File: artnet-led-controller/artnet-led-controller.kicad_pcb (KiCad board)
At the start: 2 copper layers, 100 x 70 mm, 75 parts, among them J1 USB4125-GF-A, J10 SWD_DEBUG, J2 HR911105A, J3 VBAT JST-PH-2, J5 LED_OUT_1, J6 LED_OUT_2, J7 LED_OUT_3, J8 LED_OUT_4, J9 OLED_SSD1306, SW1 SW_Push, SW2 SW_Push, SW3 SW_Push, U1 RP2040, U2 W25Q16JVSSIQ, U3 W5500, U4 SN74AHCT125, U5 TP4056, U6 MT3608, U7 AMS1117-3.3, Y1 12MHz, Y2 25MHz

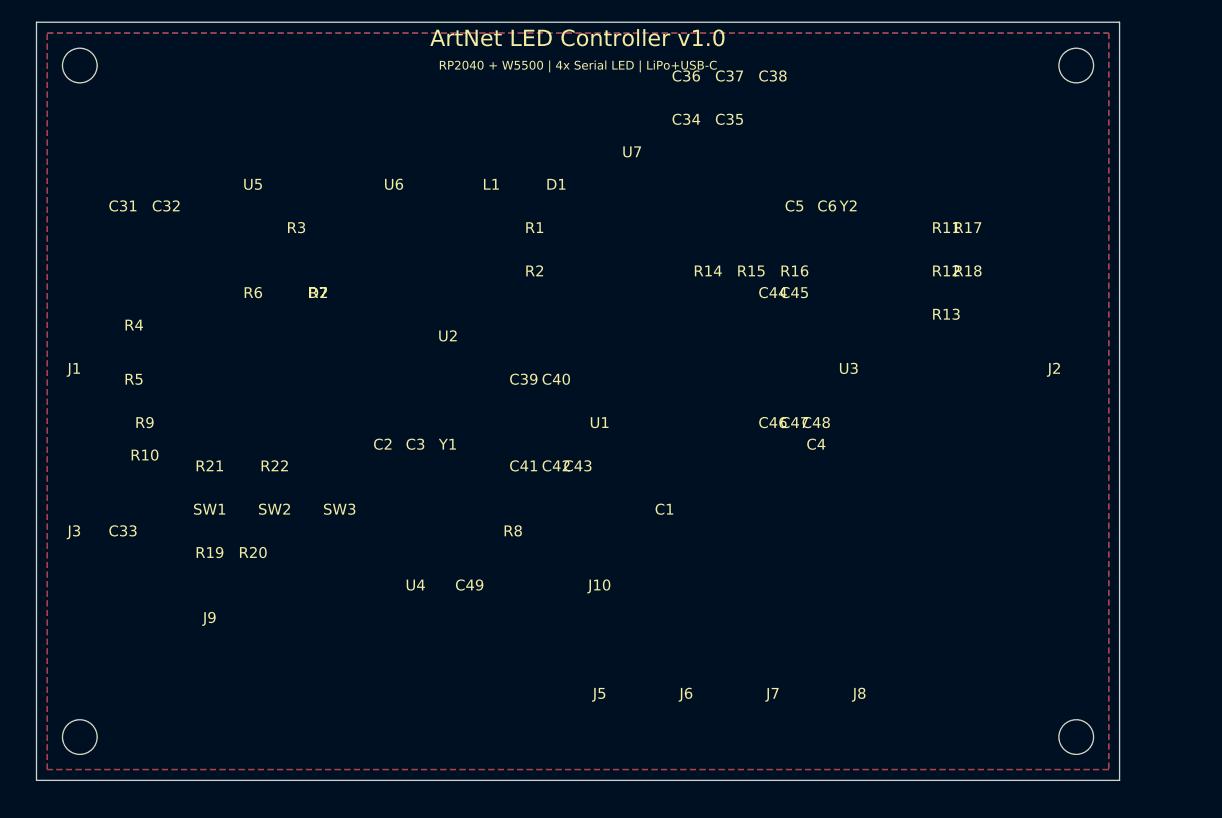
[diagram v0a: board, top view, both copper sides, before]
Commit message: Redesign controller around RP2354A
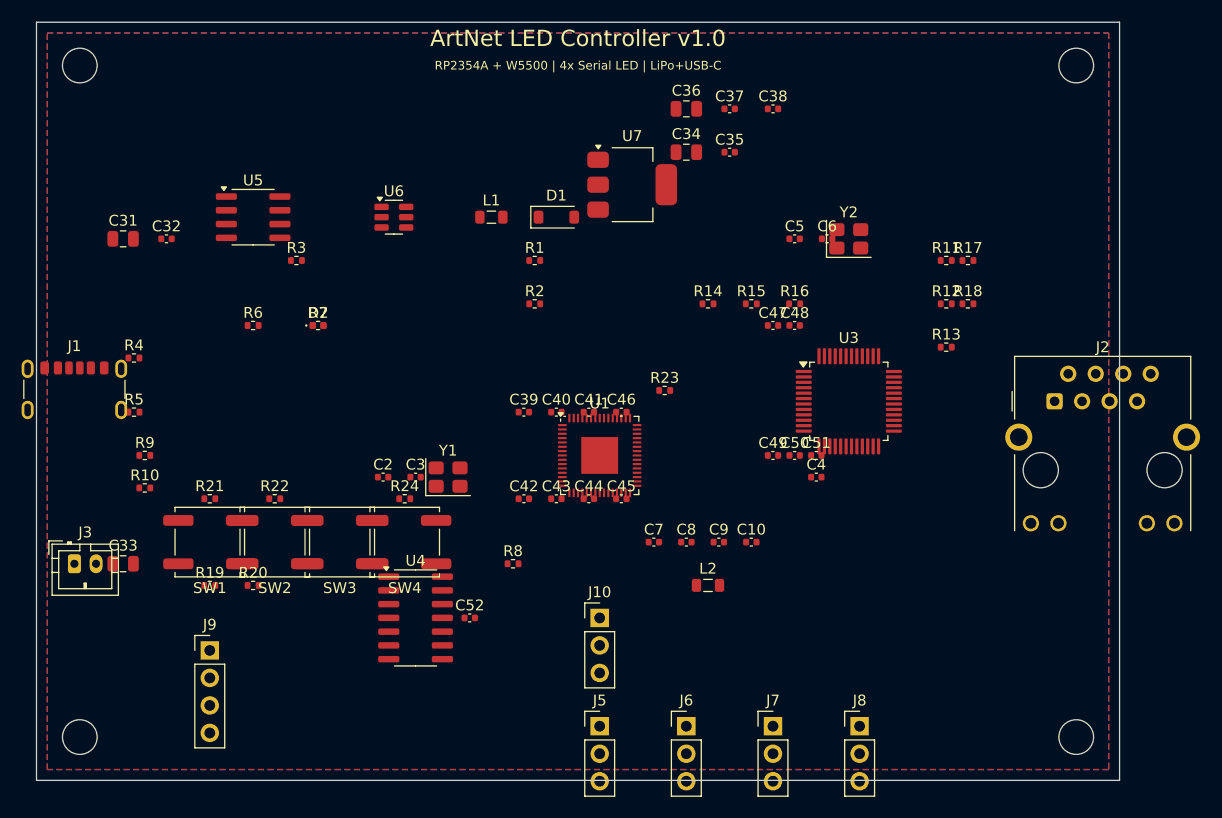
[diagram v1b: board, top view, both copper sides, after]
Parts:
- removed C1: 100nF, Capacitor_SMD:C_0402_1005Metric
- removed U2: W25Q16JVSSIQ, Package_SO:SOIC-8_3.9x4.9mm_P1.27mm
- added C10: 4.7uF, Capacitor_SMD:C_0402_1005Metric, F.Cu at (66.0, 48.0)
- added C50: 100nF, Capacitor_SMD:C_0402_1005Metric, F.Cu at (70.0, 40.0)
- added C51: 4.7uF, Capacitor_SMD:C_0402_1005Metric, F.Cu at (72.0, 40.0)
- added C52: 100nF, Capacitor_SMD:C_0402_1005Metric, F.Cu at (40.0, 55.0)
- added C7: 4.7uF, Capacitor_SMD:C_0402_1005Metric, F.Cu at (57.0, 48.0)
- added C8: 100nF, Capacitor_SMD:C_0402_1005Metric, F.Cu at (60.0, 48.0)
- added C9: 4.7uF, Capacitor_SMD:C_0402_1005Metric, F.Cu at (63.0, 48.0)
- added L2: 3.3uH, Inductor_SMD:L_0805_2012Metric, F.Cu at (62.0, 52.0)
- added R23: 33, Resistor_SMD:R_0402_1005Metric, F.Cu at (58.0, 34.0)
- added R24: 1k, Resistor_SMD:R_0402_1005Metric, F.Cu at (34.0, 44.0)
- added SW4: SW_Push, Button_Switch_SMD:SW_Push_1P1T_NO_CK_KSC7xxJ, F.Cu at (34.0, 48.0)
- C43: value 1uF -> 100nF
- C46: value 100nF -> 4.7uF
- C48: value 4.7uF -> 100nF
- J1: footprint Connector_USB:USB_C_Receptacle_GCT_USB4125_1x_1614 -> Connector_USB:USB_C_Receptacle_GCT_USB4125-xx-x_6P_TopMnt_Horizontal
- J2: footprint Connector_RJ:RJ45_Amphenol_54602-x08_Horizontal -> Connector_RJ:RJ45_Hanrun_HR911105A_Horizontal
- SW1, SW2, SW3: footprint Button_Switch_SMD:SW_Push_1P1T_NO_Vertical_Straight_PadInPin_CK_KSC741J -> Button_Switch_SMD:SW_Push_1P1T_NO_CK_KSC7xxJ
- U1: value RP2040 -> RP2354A; footprint Package_DFN_QFN:QFN-56-1EP_7x7mm_P0.4mm_EP3.2x3.2mm -> Package_DFN_QFN:QFN-60-1EP_7x7mm_P0.4mm_EP3.4x3.4mm
- moved C49 31.8 mm to (68.0, 40.0)
- moved C44 23.3 mm to (51.0, 44.0)
- moved C45 22.6 mm to (54.0, 44.0)
- moved C46 14.6 mm to (54.0, 36.0)
- moved C47 12.2 mm to (68.0, 28.0)
- moved C48 12.2 mm to (70.0, 28.0)
- moved C41 10.0 mm to (51.0, 36.0)
- moved C42 3.00 mm to (45.0, 44.0)
- moved C43 2.00 mm to (48.0, 44.0)
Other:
- board text added: "RP2354A + W5500 | 4x Serial LED | LiPo+USB-C"
- board text removed: "RP2040 + W5500 | 4x Serial LED | LiPo+USB-C"

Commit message: Clean PCB DRC and rotate RJ45
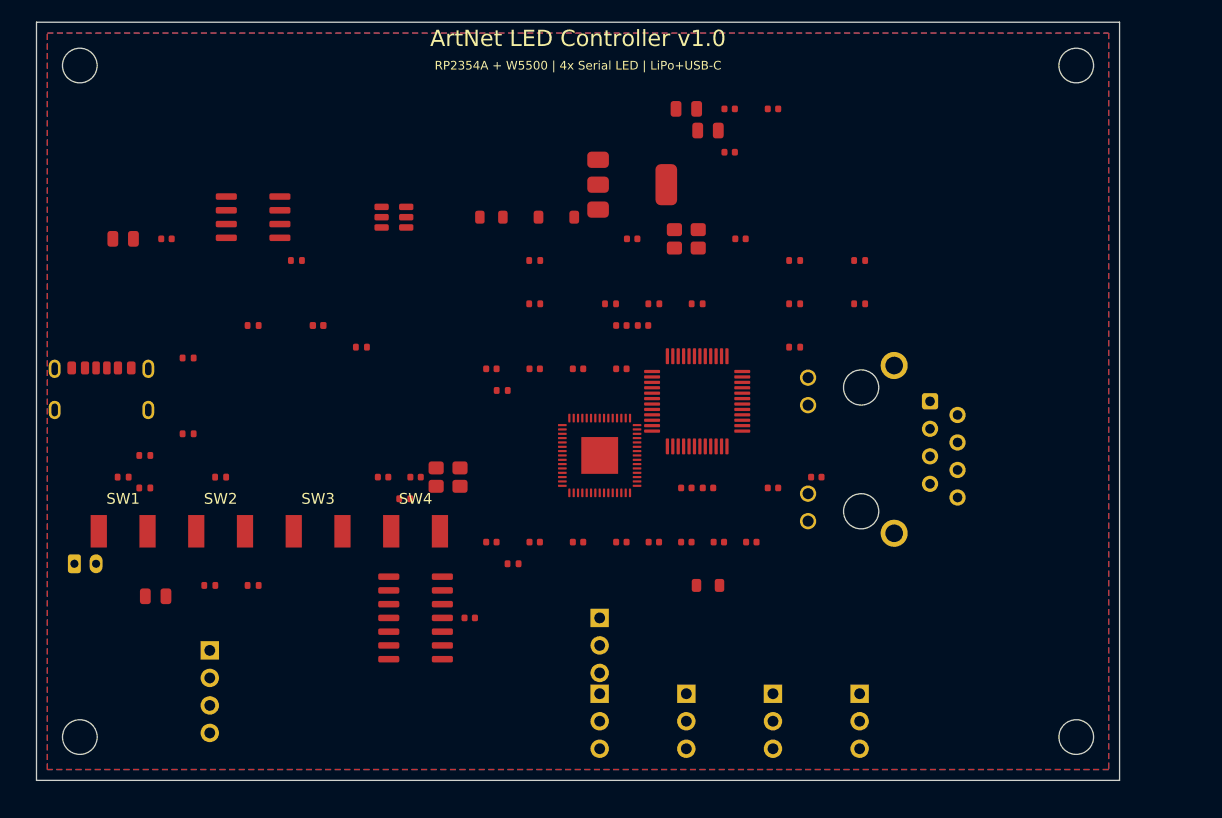
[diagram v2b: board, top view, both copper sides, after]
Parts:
- removed ? (x4): , MountingHole:MountingHole_3.2mm_M3
- added H1: MountingHole, MountingHole:MountingHole_3.2mm_M3, F.Cu at (4.00, 4.00)
- added H2: MountingHole, MountingHole:MountingHole_3.2mm_M3, F.Cu at (96.0, 4.00)
- added H3: MountingHole, MountingHole:MountingHole_3.2mm_M3, F.Cu at (4.00, 66.0)
- added H4: MountingHole, MountingHole:MountingHole_3.2mm_M3, F.Cu at (96.0, 66.0)
- moved C42 15.0 mm to (54.0, 32.0)
- moved C5 15.0 mm to (55.0, 20.0)
- moved R23 15.0 mm to (43.0, 34.0)
- moved Y2 15.0 mm to (60.0, 20.0)
- moved C47 14.0 mm to (54.0, 28.0)
- moved C48 14.0 mm to (56.0, 28.0)
- moved R11 14.0 mm to (70.0, 22.0)
- moved R12 14.0 mm to (70.0, 26.0)
- moved R13 14.0 mm to (70.0, 30.0)
- moved U3 14.0 mm to (61.0, 35.0)
- moved C46 12.0 mm to (54.0, 48.0)
- moved J2 11.5 mm to (82.5, 35.0), turned to 270 degrees
- moved R17 10.0 mm to (76.0, 22.0)
- moved R18 10.0 mm to (76.0, 26.0)
- moved R14 9.00 mm to (53.0, 26.0)
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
